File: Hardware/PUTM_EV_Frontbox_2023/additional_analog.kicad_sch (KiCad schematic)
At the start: 11 parts, among them U9 DNP

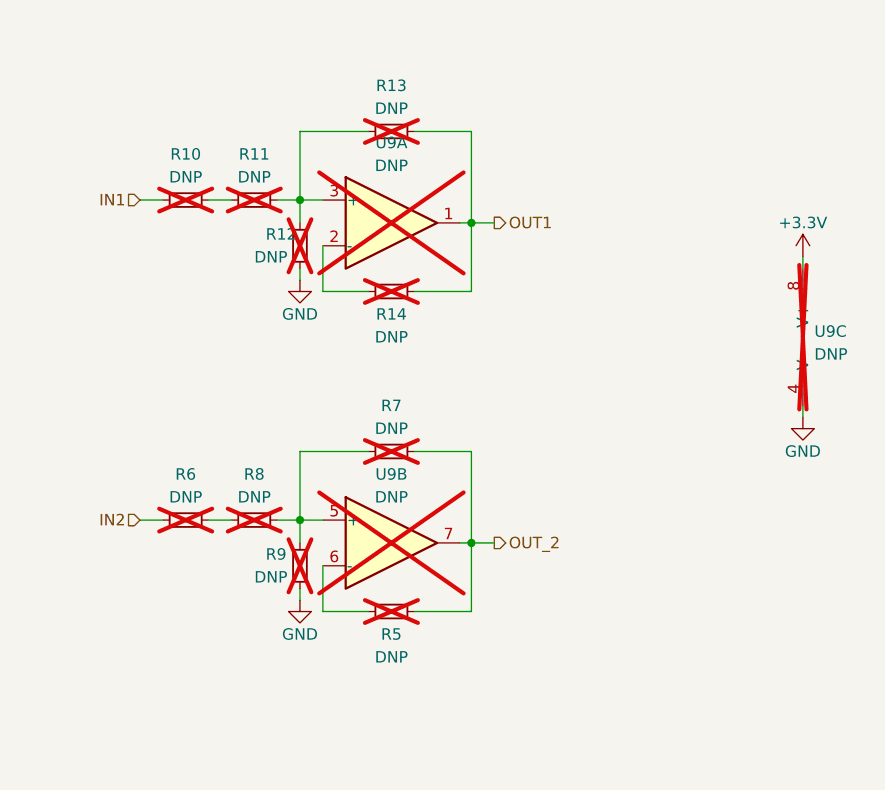
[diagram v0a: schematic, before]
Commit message: Added MCU wiring
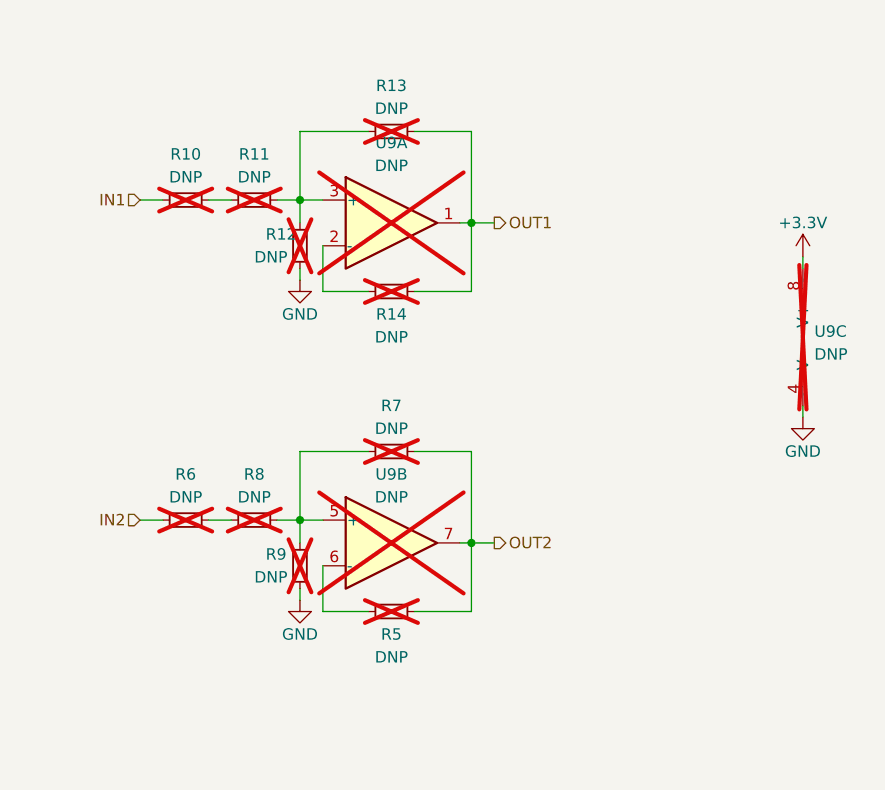
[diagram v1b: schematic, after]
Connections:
- net OUT_2 renamed OUT2
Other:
- title: Additional inputs -> Additional analog inputs
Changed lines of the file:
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@@
   (paper "A4")
   (title_block
-    (title "Additional inputs")
+    (title "Additional analog inputs")
     (date "2023-02-24")
     (rev "${REVISION}")
@@
     (effects (font (size 1.27 1.27)) (justify right))
   )
-  (hierarchical_label "OUT_2" (shape output) (at 149.86 121.92 0) (fields_autoplaced)
+  (hierarchical_label "OUT2" (shape output) (at 149.86 121.92 0) (fields_autoplaced)
     (effects (font (size 1.27 1.27)) (justify left))
   )

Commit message: Schematic ready for review
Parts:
- renumbered R10 to R48, R6 to R49, R11 to R50, R8 to R51, R12 to R52, R9 to R53, R13 to R54, R14 to R55, R7 to R56, R5 to R57, U9 to U15
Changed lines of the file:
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@@
   (title_block
     (title "Additional analog inputs")
-    (date "2023-02-24")
+    (date "2023-03-11")
     (rev "${REVISION}")
     (company "Author: Szymon Kostrubiec")
@@
   (symbol (lib_id "Device:R_Small") (at 138.43 93.98 90) (mirror x) (unit 1)
     (in_bom no) (on_board yes) (dnp yes)
-    (property "Reference" "R14" (at 138.43 96.52 90)
+    (property "Reference" "R55" (at 138.43 96.52 90)
       (effects (font (size 1.27 1.27)))
     )
@@
       (project "PUTM_EV_Frontbox_2023"
         (path "/b652b05a-4e3d-4ad1-b032-18886abe7d45/9fbfc50e-04b7-423f-b17b-8c9b93934806"
-          (reference "R14") (unit 1)
+          (reference "R55") (unit 1)
         )
       )
@@
   (symbol (lib_id "Device:R_Small") (at 138.43 129.54 90) (mirror x) (unit 1)
     (in_bom no) (on_board yes) (dnp yes)
-    (property "Reference" "R5" (at 138.43 132.08 90)
+    (property "Reference" "R57" (at 138.43 132.08 90)
       (effects (font (size 1.27 1.27)))
     )
@@
       (project "PUTM_EV_Frontbox_2023"
         (path "/b652b05a-4e3d-4ad1-b032-18886abe7d45/9fbfc50e-04b7-423f-b17b-8c9b93934806"
-          (reference "R5") (unit 1)
+          (reference "R57") (unit 1)
         )
       )
@@
   (symbol (lib_id "Device:R_Small") (at 123.19 83.82 90) (unit 1)
     (in_bom no) (on_board yes) (dnp yes) (fields_autoplaced)
-    (property "Reference" "R11" (at 123.19 78.74 90)
+    (property "Reference" "R50" (at 123.19 78.74 90)
       (effects (font (size 1.27 1.27)))
     )
@@
       (project "PUTM_EV_Frontbox_2023"
         (path "/b652b05a-4e3d-4ad1-b032-18886abe7d45/9fbfc50e-04b7-423f-b17b-8c9b93934806"
-          (reference "R11") (unit 1)
+          (reference "R50") (unit 1)
         )
       )
@@
   (symbol (lib_id "Device:R_Small") (at 128.27 124.46 0) (unit 1)
     (in_bom no) (on_board yes) (dnp yes)
-    (property "Reference" "R9" (at 124.46 123.19 0)
+    (property "Reference" "R53" (at 124.46 123.19 0)
       (effects (font (size 1.27 1.27)) (justify left))
     )
@@
       (project "PUTM_EV_Frontbox_2023"
         (path "/b652b05a-4e3d-4ad1-b032-18886abe7d45/9fbfc50e-04b7-423f-b17b-8c9b93934806"
-          (reference "R9") (unit 1)
+          (reference "R53") (unit 1)
         )
       )
@@
   (symbol (lib_id "Device:R_Small") (at 128.27 88.9 0) (unit 1)
     (in_bom no) (on_board yes) (dnp yes)
-    (property "Reference" "R12" (at 124.46 87.63 0)
+    (property "Reference" "R52" (at 124.46 87.63 0)
       (effects (font (size 1.27 1.27)) (justify left))
     )
@@
       (project "PUTM_EV_Frontbox_2023"
         (path "/b652b05a-4e3d-4ad1-b032-18886abe7d45/9fbfc50e-04b7-423f-b17b-8c9b93934806"
-          (reference "R12") (unit 1)
+          (reference "R52") (unit 1)
         )
       )
@@
   (symbol (lib_id "power:GND") (at 128.27 128.27 0) (unit 1)
     (in_bom yes) (on_board yes) (dnp no)
-    (property "Reference" "#PWR058" (at 128.27 134.62 0)
+    (property "Reference" "#PWR0107" (at 128.27 134.62 0)
       (effects (font (size 1.27 1.27)) hide)
     )
@@
       (project "PUTM_EV_Frontbox_2023"
         (path "/b652b05a-4e3d-4ad1-b032-18886abe7d45/9fbfc50e-04b7-423f-b17b-8c9b93934806"
-          (reference "#PWR058") (unit 1)
+          (reference "#PWR0107") (unit 1)
         )
       )
@@
   (symbol (lib_id "Device:R_Small") (at 123.19 119.38 90) (unit 1)
     (in_bom no) (on_board yes) (dnp yes) (fields_autoplaced)
-    (property "Reference" "R8" (at 123.19 114.3 90)
+    (property "Reference" "R51" (at 123.19 114.3 90)
       (effects (font (size 1.27 1.27)))
     )
@@
       (project "PUTM_EV_Frontbox_2023"
         (path "/b652b05a-4e3d-4ad1-b032-18886abe7d45/9fbfc50e-04b7-423f-b17b-8c9b93934806"
-          (reference "R8") (unit 1)
+          (reference "R51") (unit 1)
         )
       )
@@
   (symbol (lib_id "Device:R_Small") (at 115.57 83.82 90) (unit 1)
     (in_bom no) (on_board yes) (dnp yes) (fields_autoplaced)
-    (property "Reference" "R10" (at 115.57 78.74 90)
+    (property "Reference" "R48" (at 115.57 78.74 90)
       (effects (font (size 1.27 1.27)))
     )
@@
       (project "PUTM_EV_Frontbox_2023"
         (path "/b652b05a-4e3d-4ad1-b032-18886abe7d45/9fbfc50e-04b7-423f-b17b-8c9b93934806"
-          (reference "R10") (unit 1)
+          (reference "R48") (unit 1)
         )
       )
@@
   (symbol (lib_id "Amplifier_Operational:TLV9062") (at 138.43 121.92 0) (unit 2)
     (in_bom no) (on_board yes) (dnp yes)
-    (property "Reference" "U9" (at 138.43 114.3 0)
+    (property "Reference" "U15" (at 138.43 114.3 0)
       (effects (font (size 1.27 1.27)))
     )
@@
       (project "PUTM_EV_Frontbox_2023"
         (path "/b652b05a-4e3d-4ad1-b032-18886abe7d45/9fbfc50e-04b7-423f-b17b-8c9b93934806"
-          (reference "U9") (unit 2)
+          (reference "U15") (unit 2)
         )
       )
@@
   (symbol (lib_id "Device:R_Small") (at 138.43 111.76 270) (unit 1)
     (in_bom no) (on_board yes) (dnp yes) (fields_autoplaced)
-    (property "Reference" "R7" (at 138.43 106.68 90)
+    (property "Reference" "R56" (at 138.43 106.68 90)
       (effects (font (size 1.27 1.27)))
     )
@@
       (project "PUTM_EV_Frontbox_2023"
         (path "/b652b05a-4e3d-4ad1-b032-18886abe7d45/9fbfc50e-04b7-423f-b17b-8c9b93934806"
-          (reference "R7") (unit 1)
+          (reference "R56") (unit 1)
         )
       )
@@
   (symbol (lib_id "Amplifier_Operational:TLV9062") (at 186.69 99.06 0) (unit 3)
     (in_bom no) (on_board yes) (dnp yes) (fields_autoplaced)
-    (property "Reference" "U9" (at 185.42 98.425 0)
+    (property "Reference" "U15" (at 185.42 98.425 0)
       (effects (font (size 1.27 1.27)) (justify left))
     )
@@
       (project "PUTM_EV_Frontbox_2023"
         (path "/b652b05a-4e3d-4ad1-b032-18886abe7d45/9fbfc50e-04b7-423f-b17b-8c9b93934806"
-          (reference "U9") (unit 3)
+          (reference "U15") (unit 3)
         )
       )
@@
   (symbol (lib_id "power:GND") (at 128.27 92.71 0) (unit 1)
     (in_bom yes) (on_board yes) (dnp no)
-    (property "Reference" "#PWR059" (at 128.27 99.06 0)
+    (property "Reference" "#PWR0106" (at 128.27 99.06 0)
       (effects (font (size 1.27 1.27)) hide)
     )
@@
       (project "PUTM_EV_Frontbox_2023"
         (path "/b652b05a-4e3d-4ad1-b032-18886abe7d45/9fbfc50e-04b7-423f-b17b-8c9b93934806"
-          (reference "#PWR059") (unit 1)
+          (reference "#PWR0106") (unit 1)
         )
       )
@@
   (symbol (lib_id "Amplifier_Operational:TLV9062") (at 138.43 86.36 0) (unit 1)
     (in_bom no) (on_board yes) (dnp yes) (fields_autoplaced)
-    (property "Reference" "U9" (at 138.43 77.47 0)
+    (property "Reference" "U15" (at 138.43 77.47 0)
       (effects (font (size 1.27 1.27)))
     )
@@
       (project "PUTM_EV_Frontbox_2023"
         (path "/b652b05a-4e3d-4ad1-b032-18886abe7d45/9fbfc50e-04b7-423f-b17b-8c9b93934806"
-          (reference "U9") (unit 1)
+          (reference "U15") (unit 1)
         )
       )
@@
   (symbol (lib_id "power:+3.3V") (at 184.15 90.17 0) (unit 1)
     (in_bom yes) (on_board yes) (dnp no) (fields_autoplaced)
-    (property "Reference" "#PWR056" (at 184.15 93.98 0)
+    (property "Reference" "#PWR0108" (at 184.15 93.98 0)
       (effects (font (size 1.27 1.27)) hide)
     )
@@
       (project "PUTM_EV_Frontbox_2023"
         (path "/b652b05a-4e3d-4ad1-b032-18886abe7d45/9fbfc50e-04b7-423f-b17b-8c9b93934806"
-          (reference "#PWR056") (unit 1)
+          (reference "#PWR0108") (unit 1)
         )
       )
@@
   (symbol (lib_id "Device:R_Small") (at 138.43 76.2 270) (unit 1)
     (in_bom no) (on_board yes) (dnp yes) (fields_autoplaced)
-    (property "Reference" "R13" (at 138.43 71.12 90)
+    (property "Reference" "R54" (at 138.43 71.12 90)
       (effects (font (size 1.27 1.27)))
     )
@@
       (project "PUTM_EV_Frontbox_2023"
         (path "/b652b05a-4e3d-4ad1-b032-18886abe7d45/9fbfc50e-04b7-423f-b17b-8c9b93934806"
-          (reference "R13") (unit 1)
+          (reference "R54") (unit 1)
         )
       )
@@
   (symbol (lib_id "power:GND") (at 184.15 107.95 0) (unit 1)
     (in_bom yes) (on_board yes) (dnp no)
-    (property "Reference" "#PWR057" (at 184.15 114.3 0)
+    (property "Reference" "#PWR0109" (at 184.15 114.3 0)
       (effects (font (size 1.27 1.27)) hide)
     )
@@
       (project "PUTM_EV_Frontbox_2023"
         (path "/b652b05a-4e3d-4ad1-b032-18886abe7d45/9fbfc50e-04b7-423f-b17b-8c9b93934806"
-          (reference "#PWR057") (unit 1)
+          (reference "#PWR0109") (unit 1)
         )
       )
@@
   (symbol (lib_id "Device:R_Small") (at 115.57 119.38 90) (unit 1)
     (in_bom no) (on_board yes) (dnp yes) (fields_autoplaced)
-    (property "Reference" "R6" (at 115.57 114.3 90)
+    (property "Reference" "R49" (at 115.57 114.3 90)
       (effects (font (size 1.27 1.27)))
     )
@@
       (project "PUTM_EV_Frontbox_2023"
         (path "/b652b05a-4e3d-4ad1-b032-18886abe7d45/9fbfc50e-04b7-423f-b17b-8c9b93934806"
-          (reference "R6") (unit 1)
-        )
-      )
+          (reference "R49") (unit 1)
+        )
+      )

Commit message: Fixed all issues
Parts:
- removed unit 2 of U15
- added R90, R91: DNP, symbol Device:R_Small
- added U21: DNP, symbol Amplifier_Operational:TLV9062
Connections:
- net GND: now also R56.2, R90.2
- net OUT2: now also R57.1, R91.2, U21.1; no longer R56.1, R57.2
- net at R55.1, U15.2 (-): now also R90.1
- net at R51.2, R53.1: now also R57.2, U21.3 (+); no longer R56.2
- new net: R56.1, R91.1, U21.2 (-)
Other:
- note added: "This is a 'blanket' op amp circuit, which can be made into SK filter, noninvering or differential amplifier when the need arises."
- moved on the sheet: R48, R50, R52, U15C

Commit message: Schematic modified, footprints assigned
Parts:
- R48, R49, R50, R51, R52, R53, R54, R55, R56, R57, R90, R91: footprint (none) -> Resistor_SMD:R_0603_1608Metric
- U15, U21: footprint (none) -> Package_TO_SOT_SMD:TSOT-23-8_HandSoldering
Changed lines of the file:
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@@
       (effects (font (size 1.27 1.27)))
     )
-    (property "Footprint" "" (at 138.43 93.98 0)
+    (property "Footprint" "Resistor_SMD:R_0603_1608Metric" (at 138.43 93.98 0)
       (effects (font (size 1.27 1.27)) hide)
     )
@@
       (effects (font (size 1.27 1.27)))
     )
-    (property "Footprint" "" (at 115.57 83.82 0)
+    (property "Footprint" "Resistor_SMD:R_0603_1608Metric" (at 115.57 83.82 0)
       (effects (font (size 1.27 1.27)) hide)
     )
@@
       (effects (font (size 1.27 1.27)))
     )
-    (property "Footprint" "" (at 138.43 115.57 0)
+    (property "Footprint" "Resistor_SMD:R_0603_1608Metric" (at 138.43 115.57 0)
       (effects (font (size 1.27 1.27)) hide)
     )
@@
       (effects (font (size 1.27 1.27)))
     )
-    (property "Footprint" "" (at 115.57 123.19 0)
+    (property "Footprint" "Resistor_SMD:R_0603_1608Metric" (at 115.57 123.19 0)
       (effects (font (size 1.27 1.27)) hide)
     )
@@
       (effects (font (size 1.27 1.27)))
     )
-    (property "Footprint" "" (at 138.43 125.73 0)
+    (property "Footprint" "Package_TO_SOT_SMD:TSOT-23-8_HandSoldering" (at 138.43 125.73 0)
       (effects (font (size 1.27 1.27)) hide)
     )
@@
       (effects (font (size 1.27 1.27)) (justify left))
     )
-    (property "Footprint" "" (at 130.81 138.43 0)
+    (property "Footprint" "Resistor_SMD:R_0603_1608Metric" (at 130.81 138.43 0)
       (effects (font (size 1.27 1.27)) hide)
     )
@@
       (effects (font (size 1.27 1.27)) (justify left))
     )
-    (property "Footprint" "" (at 120.65 88.9 0)
+    (property "Footprint" "Resistor_SMD:R_0603_1608Metric" (at 120.65 88.9 0)
       (effects (font (size 1.27 1.27)) hide)
     )
@@
       (effects (font (size 1.27 1.27)))
     )
-    (property "Footprint" "" (at 107.95 123.19 0)
+    (property "Footprint" "Resistor_SMD:R_0603_1608Metric" (at 107.95 123.19 0)
       (effects (font (size 1.27 1.27)) hide)
     )
@@
       (effects (font (size 1.27 1.27)))
     )
-    (property "Footprint" "" (at 107.95 83.82 0)
+    (property "Footprint" "Resistor_SMD:R_0603_1608Metric" (at 107.95 83.82 0)
       (effects (font (size 1.27 1.27)) hide)
     )
@@
       (effects (font (size 1.27 1.27)) (justify left))
     )
-    (property "Footprint" "" (at 120.65 128.27 0)
+    (property "Footprint" "Resistor_SMD:R_0603_1608Metric" (at 120.65 128.27 0)
       (effects (font (size 1.27 1.27)) hide)
     )
@@
       (effects (font (size 1.27 1.27)) (justify left))
     )
-    (property "Footprint" "" (at 130.81 99.06 0)
+    (property "Footprint" "Resistor_SMD:R_0603_1608Metric" (at 130.81 99.06 0)
       (effects (font (size 1.27 1.27)) hide)
     )
@@
       (effects (font (size 1.27 1.27)) (justify left))
     )
-    (property "Footprint" "" (at 181.61 105.41 0)
+    (property "Footprint" "Package_TO_SOT_SMD:TSOT-23-8_HandSoldering" (at 181.61 105.41 0)
       (effects (font (size 1.27 1.27)) hide)
     )
@@
       (effects (font (size 1.27 1.27)))
     )
-    (property "Footprint" "" (at 138.43 86.36 0)
+    (property "Footprint" "Package_TO_SOT_SMD:TSOT-23-8_HandSoldering" (at 138.43 86.36 0)
       (effects (font (size 1.27 1.27)) hide)
     )
@@
       (effects (font (size 1.27 1.27)))
     )
-    (property "Footprint" "" (at 138.43 133.35 0)
+    (property "Footprint" "Resistor_SMD:R_0603_1608Metric" (at 138.43 133.35 0)
       (effects (font (size 1.27 1.27)) hide)
     )
@@
       (effects (font (size 1.27 1.27)))
     )
-    (property "Footprint" "" (at 138.43 76.2 0)
-      (effects (font (size 1.27 1.27)) hide)
-    )
+    (property "Footprint" "Resistor_SMD:R_0603_1608Metric" (at 138.43 76.2 0)
+      (effects (font (size 1.27 1.27)) hide)
+    )
